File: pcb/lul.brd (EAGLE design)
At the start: 90 x 96 mm, 86 parts, among them IC1 STM32F072C8T6, IC2 REG1117, IC3 74AHCT1G08DBV, U1 UG-2864HSWEG01

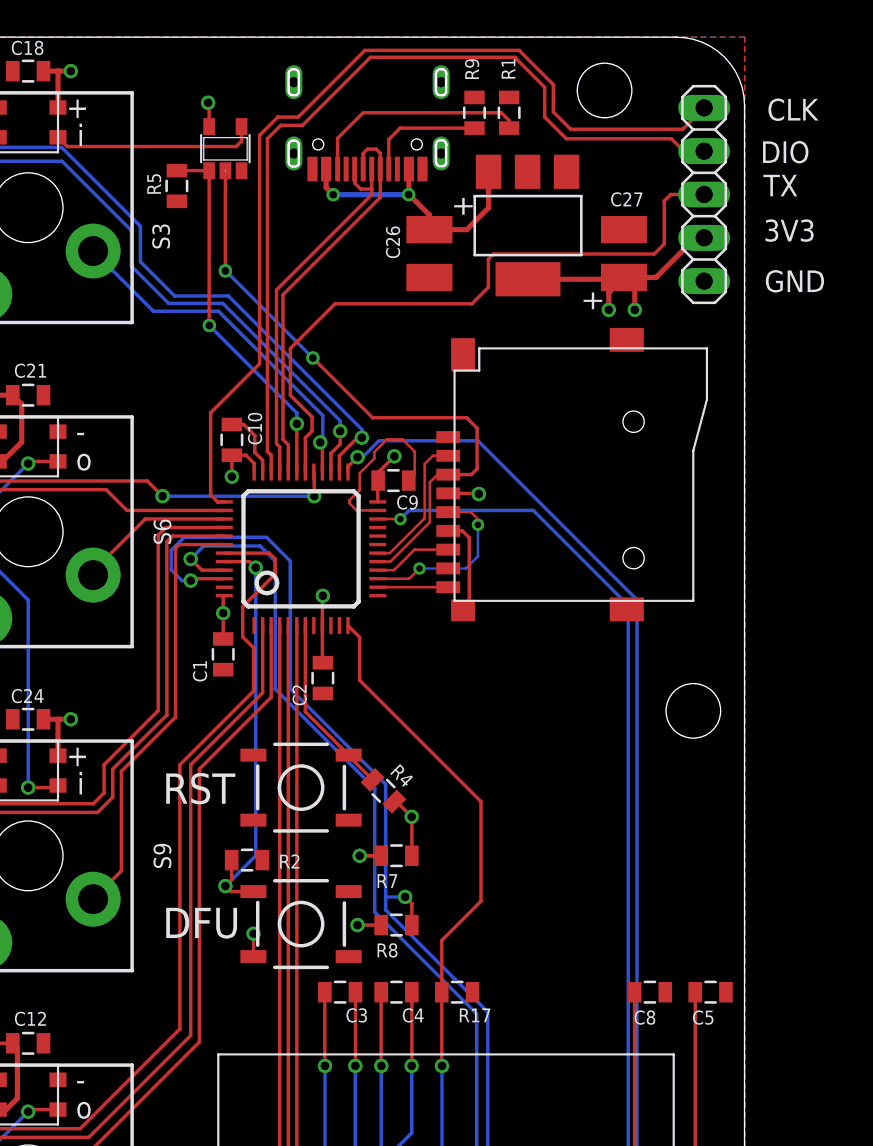
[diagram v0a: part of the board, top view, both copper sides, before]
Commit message: replaced DFU and RST button
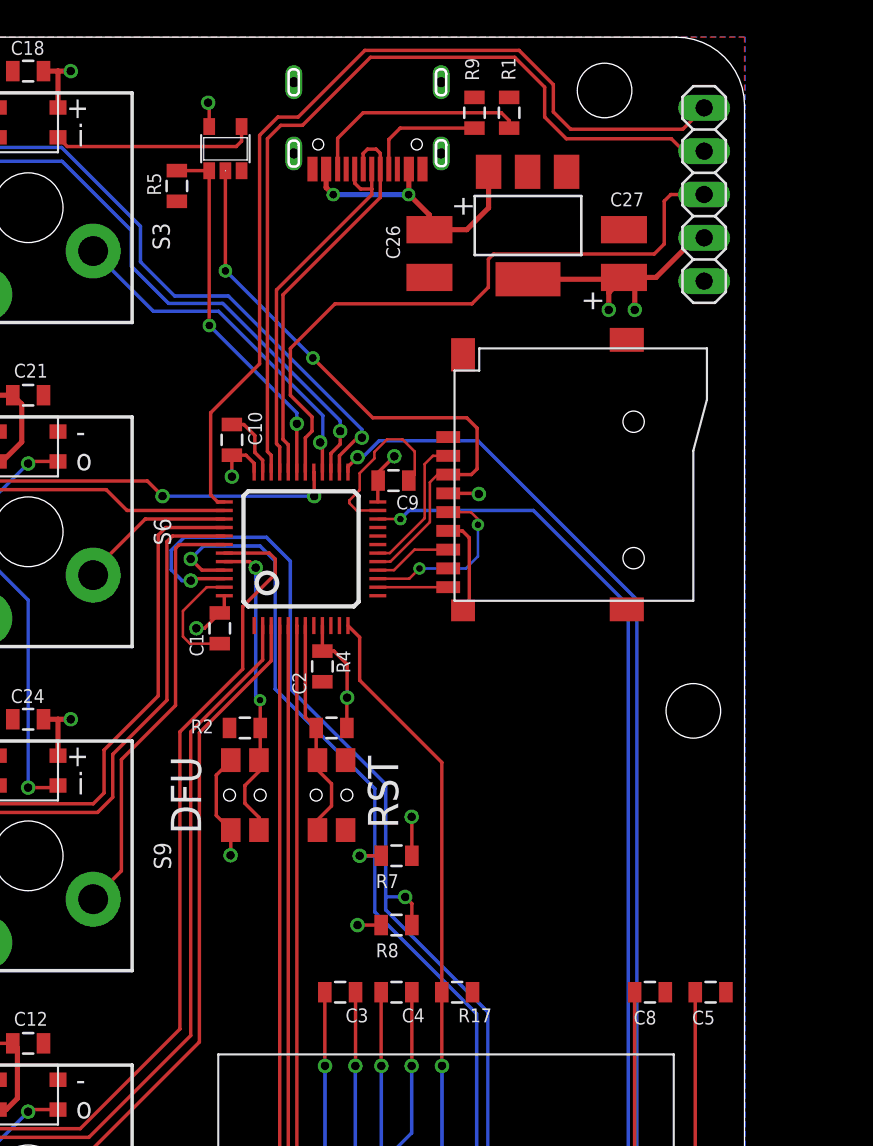
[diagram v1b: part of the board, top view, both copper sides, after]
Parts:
- removed S21, S22: TAC_SWITCHSMD, clock:TACTILE-SWITCH-SMD
- added SW1, SW2: 324_SW324_SWITCH_FOOT_HOLE, 3pos_slide_switch:342_SWICH_FOOT_HOLE
- moved R2 7.75 mm to (60.7, 55.5), turned to 0 degrees
- moved R4 4.78 mm to (65.8, 55.5), turned to 0 degrees
- moved C1 1.54 mm to (59.2, 61.3)
- moved C2 0.69 mm to (65.3, 59.1)
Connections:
- net +3V3: now also SW1.P$1, SW1.P$4; no longer S22.3
- net GND: now also SW2.P$2, SW2.P$3; no longer S21.4
- net N$2: now also SW1.P$2, SW1.P$3; no longer S22.1
- net RST: now also SW2.P$1, SW2.P$4; no longer S21.2
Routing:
- net +3V3: track 117.8 -> 124.7 mm
- net GND: track 48.6 -> 55.4 mm
- net N$2: track 24.8 -> 18.1 mm
- net RST: track 10.7 -> 13.0 mm
- net OLED_RESET: track 45.2 -> 43.3 mm
- net SW10: track 81.3 -> 80.8 mm
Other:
- board text added: "dekuNukem PT2 JUN19"
- board text removed: "dekuNukem 2017"

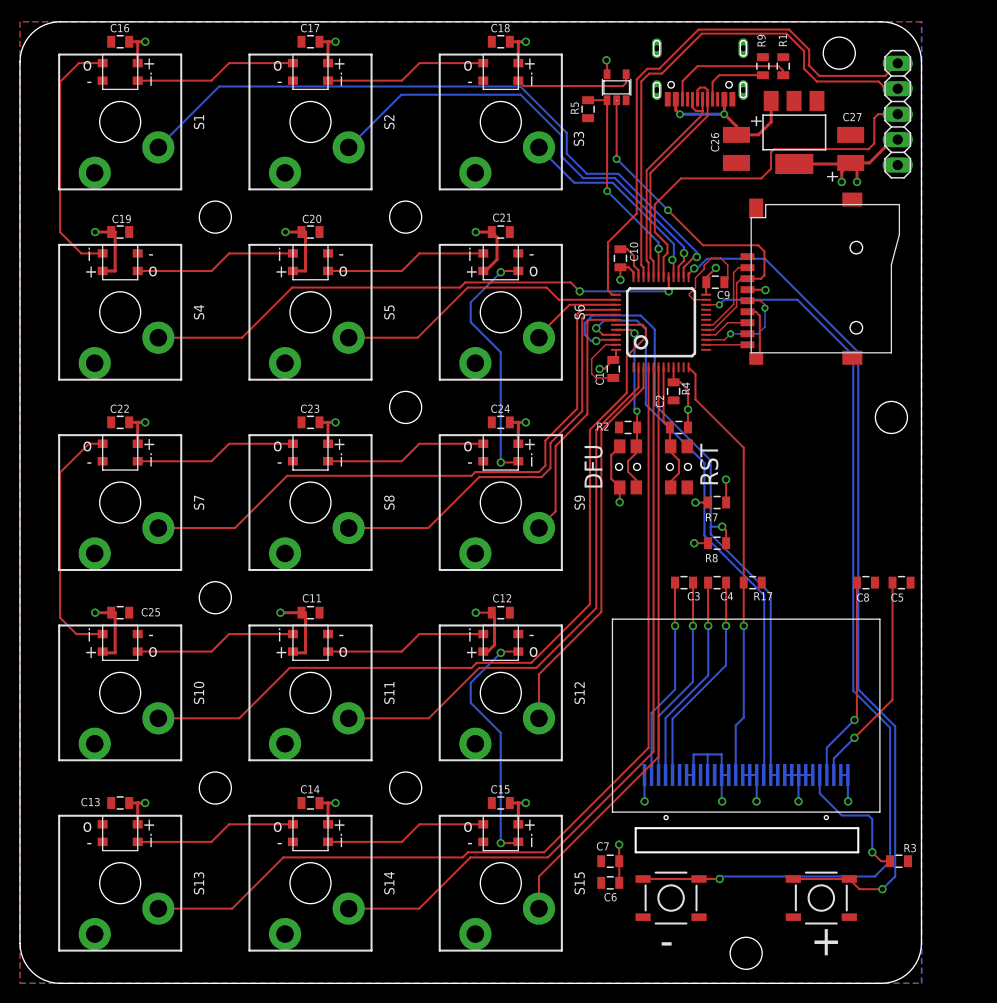
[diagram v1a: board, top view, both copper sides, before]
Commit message: new oled socket
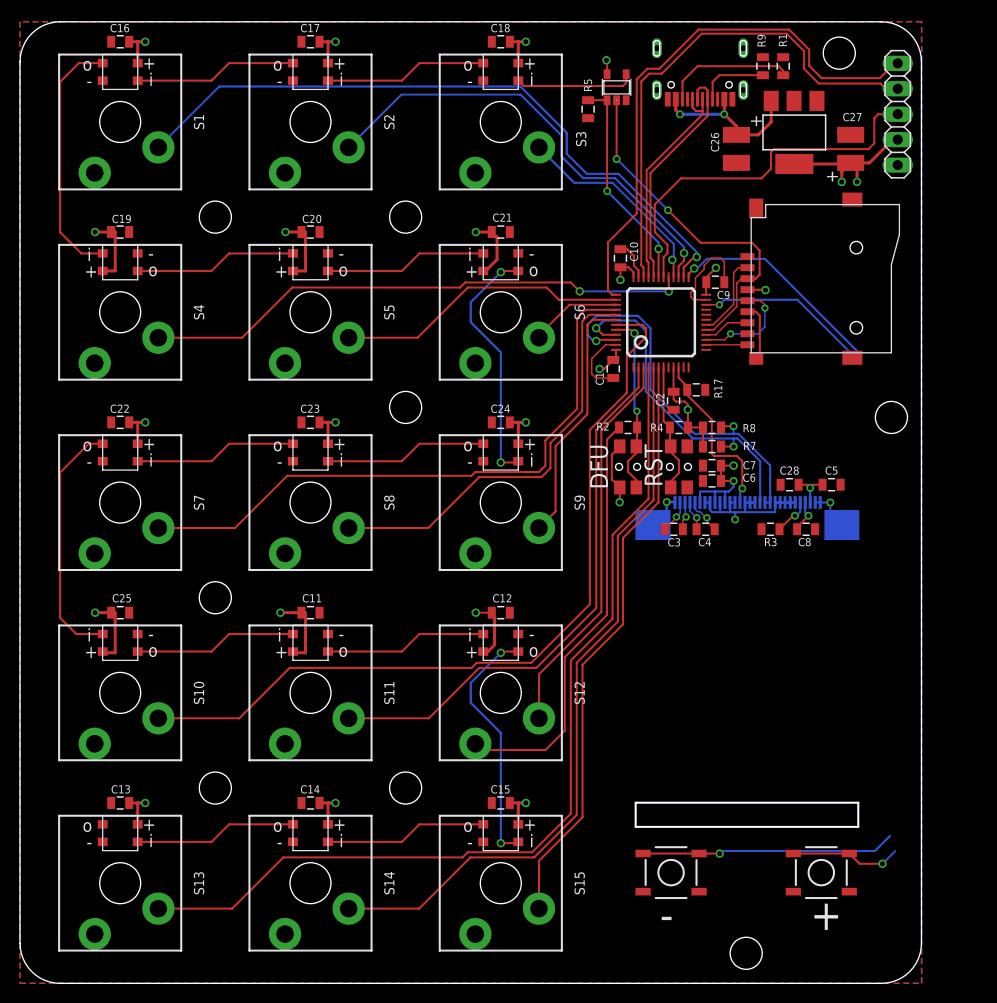
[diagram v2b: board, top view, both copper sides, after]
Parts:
- added C28: 1uF, clock:0805@1
- C7: value 1uF -> 2.2uF
- U1: device lul:UG-2864HSWEG01_0.96IN_WRAPAROUND -> lul:LUL_UG-2864HSWEG01_1.3_WRAPAROUND
- moved C6 41.4 mm to (69.1, 50.2)
- moved C7 40.8 mm to (69.1, 51.7)
- moved R3 35.5 mm to (74.9, 45.3), turned to 0 degrees
- moved U1 26.0 mm to (72.6, 48.0)
- moved R17 20.1 mm to (67.5, 59.3)
- moved C5 12.0 mm to (81.0, 49.8)
- moved R8 11.6 mm to (69.1, 55.5)
- moved C8 8.01 mm to (78.5, 45.3)
- moved R7 5.61 mm to (69.1, 53.6), turned to 180 degrees
- moved C4 5.46 mm to (68.5, 45.3)
- moved C3 5.43 mm to (65.3, 45.3)
- moved S19 2.54 mm to (80.0, 11.1)
- moved S20 2.54 mm to (65.0, 11.1)
- moved C2 0.94 mm to (65.3, 58.2)
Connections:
- net GND: now also C28.1, U1.31, U1.32
- net N$11: now also C28.2
- net OLED_RESET: now also IC1.10; no longer IC1.12
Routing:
- net BUTTON1: track 86.7 -> 32.9 mm
- net BUTTON2: track 94.6 -> 42.6 mm
- net GND: track 55.4 -> 92.8 mm, vias 5 -> 3
- net SDA: track 65.4 -> 38.8 mm
- net OLED_RESET: track 43.3 -> 17.6 mm
- net SCL: track 59.4 -> 34.5 mm
- net N$6: track 21.0 -> 2.95 mm
- net N$5: track 20.6 -> 2.84 mm
- net N$7: track 21.4 -> 3.66 mm
- net N$11: track 21.6 -> 4.12 mm
- net N$12: track 20.4 -> 3.27 mm
- net N$4: track 20.2 -> 3.29 mm
- net N$3: track 13.6 -> 3.72 mm
- net +3V3: track 124.7 -> 132.2 mm, vias 27 -> 26
- net SPI_MOSI: track 36.3 -> 35.3 mm
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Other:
- outline, holes or cut-outs redrawn

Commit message: new buttons
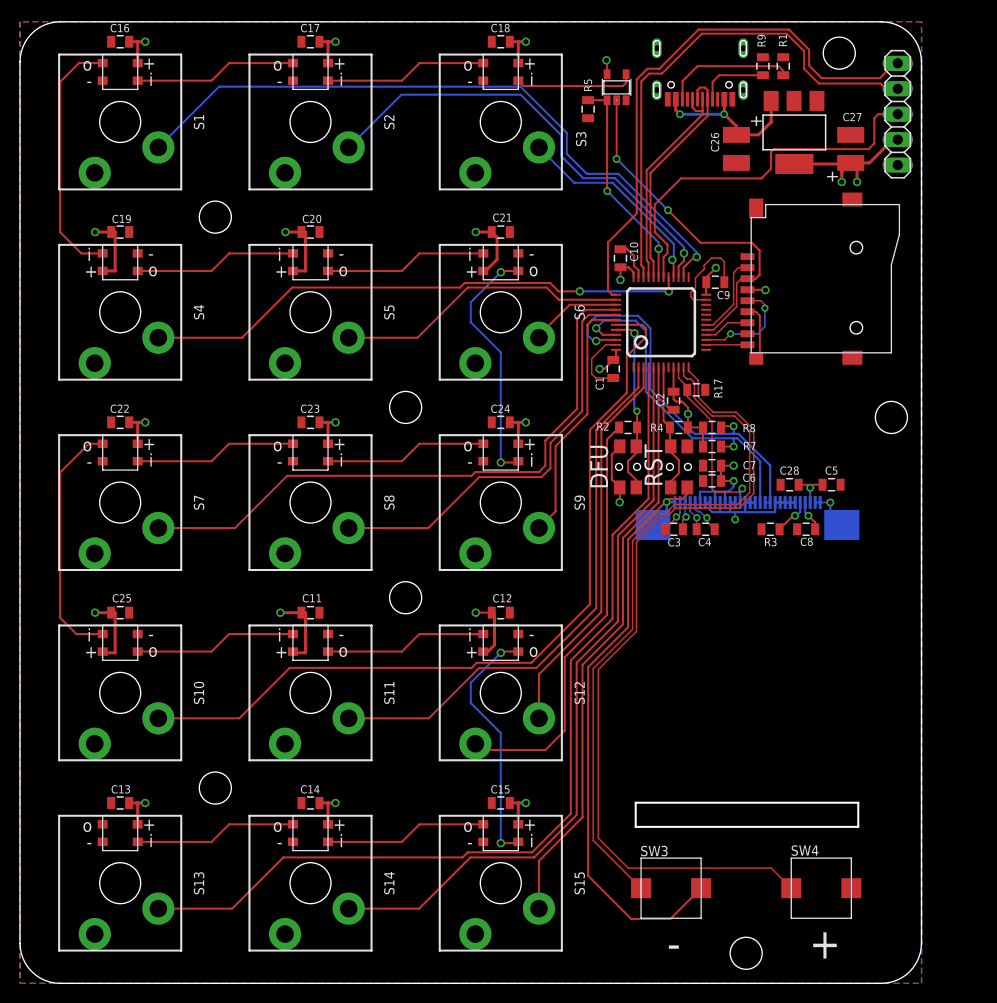
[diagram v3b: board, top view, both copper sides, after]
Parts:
- removed S19, S20: TAC_SWITCHSMD, clock:TACTILE-SWITCH-SMD
- removed U$12, U$13: M3_MOUNTING_HOLE, clock:M3_MOUNTING_HOLE_PACK
- added SW3, SW4: 6X6_SW, lul:6X6_SW_FOOT
- moved U$16 19.0 mm to (38.5, 38.5)
- turned C8 to 0 degrees
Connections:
- net BUTTON1: now also IC1.11, SW3.P$1; no longer IC1.25, S19.1, S19.2
- net BUTTON2: now also IC1.12, SW4.P$1; no longer IC1.22, S20.1, S20.2
- net GND: now also SW3.P$2, SW4.P$2; no longer S19.3, S19.4, S20.3, S20.4
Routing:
- net GND: track 92.8 -> 150.8 mm
- net BUTTON2: track 42.6 -> 82.8 mm, vias 2 -> 0
- net BUTTON1: track 32.9 -> 68.7 mm, vias 2 -> 0
- net OLED_RESET: track 17.6 -> 18.3 mm

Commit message: clean up main folder
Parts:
- C1, C10, C11, C12, C13, C14, C15, C16, C17, C18, C19, C2, C20, C21, C22, C23, C24, C25, C9: value 0.1uF -> 100nF
- C8: value 2.2uF/16V -> 2.2uF
- R2, R4, R5: value 10k -> 10K
- R7, R8: value 4K7 -> 5.1K
- S1, S10, S11, S12, S13, S14, S15, S2, S3, S4, S5, S6, S7, S8, S9: value MOMENTARY-SWITCH-SPST-LED-PTH-CHERRY -> CHERRY-MX-LED; device lul:CHERRY-MX-LED -> SparkFun-Cherry-MX-Switch-Breakout:CHERRY-MX-LED
- moved U$8 5.07 mm to (67.9, 92.2)
- moved U$9 1.41 mm to (86.0, 57.5)
- moved U$14 1.00 mm to (72.5, 4.00)
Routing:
- net SW1: track 67.5 -> 69.4 mm
- net SW2: track 46.4 -> 48.2 mm
- net GND: track 150.8 -> 149.1 mm
- net SW9: track 25.3 -> 26.2 mm
- net N$17: track 25.2 -> 26.0 mm
- net N$23: track 24.9 -> 25.7 mm
- net SW6: track 9.19 -> 9.83 mm
- net SW15: track 59.0 -> 59.5 mm
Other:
- board text added: "git.io/kbord"

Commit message: adjust components
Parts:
- moved C3 4.72 mm to (69.1, 48.1)
- moved C4 4.64 mm to (72.2, 48.1), turned to 0 degrees
- moved R3 2.90 mm to (75.7, 48.1)
- moved C8 2.81 mm to (78.7, 48.1)
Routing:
- net N$6: track 2.95 -> 8.59 mm
- net N$5: track 2.84 -> 5.84 mm
- net BUTTON1: track 68.7 -> 71.0 mm
- net BUTTON2: track 82.8 -> 85.1 mm
- net N$7: track 3.66 -> 5.70 mm
- net N$4: track 3.29 -> 5.19 mm

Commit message: new pcb ready for fab
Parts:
- removed C26: 47uF, clock:C1210
- added C29: 100nF, clock:0805@1
- moved U$10 0.72 mm to (82.5, 93.0)
- moved U$9 0.50 mm to (86.5, 57.5)
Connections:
- net GND: now also C29.1; no longer C26.2
- net N$1: now also C29.2; no longer C26.1
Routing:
- net N$1: track 16.4 -> 13.6 mm
- net UART1_TX: track 38.3 -> 39.1 mm
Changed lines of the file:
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@@
 <setting verticaltext="up"/>
 </settings>
-<grid distance="1" unitdist="mil" unit="mil" style="lines" multiple="1" display="yes" altdistance="5" altunitdist="mil" altunit="mil"/>
+<grid distance="1" unitdist="mil" unit="mm" style="lines" multiple="1" display="yes" altdistance="5" altunitdist="mil" altunit="mil"/>
 <layers>
 <layer number="1" name="Top" color="4" fill="1" visible="yes" active="yes"/>
@@
 <text x="57.8104" y="51.5874" size="1.778" layer="25" rot="R90" align="center">DFU</text>
 <text x="63.246" y="51.689" size="1.778" layer="25" rot="R270" align="center">RST</text>
-<text x="80.3656" y="4" size="3.048" layer="25" align="center">+</text>
-<text x="65.278" y="4" size="3.048" layer="25" align="center">-</text>
+<text x="80.3656" y="4.508" size="3.048" layer="25" align="center">+</text>
+<text x="65.278" y="4.508" size="3.048" layer="25" align="center">-</text>
 <text x="88.646" y="66.7766" size="2.1844" layer="26" rot="MR0">dekuNukem
 PT2 JUN19</text>
@@
 </element>
 <element name="C8" library="clock" package="0805@1" value="2.2uF" x="78.74" y="48.133" smashed="yes">
-<attribute name="NAME" x="79.4258" y="46.1391" size="0.8128" layer="25" rot="R180"/>
+<attribute name="NAME" x="82.9056" y="48.4251" size="0.8128" layer="25" rot="R180"/>
 </element>
 <element name="C6" library="clock" package="0805@1" value="1uF" x="69.088" y="50.165" smashed="yes">
@@
 </element>
 <element name="U$7" library="clock" package="M3_MOUNTING_HOLE_PACK" value="M3_MOUNTING_HOLE" x="19.5" y="19.5"/>
-<element name="U$9" library="clock" package="M3_MOUNTING_HOLE_PACK" value="M3_MOUNTING_HOLE" x="86" y="57.5"/>
-<element name="U$10" library="clock" package="M3_MOUNTING_HOLE_PACK" value="M3_MOUNTING_HOLE" x="81.795" y="92.873"/>
+<element name="U$9" library="clock" package="M3_MOUNTING_HOLE_PACK" value="M3_MOUNTING_HOLE" x="86.5" y="57.5"/>
+<element name="U$10" library="clock" package="M3_MOUNTING_HOLE_PACK" value="M3_MOUNTING_HOLE" x="82.5" y="93"/>
 <element name="U$11" library="clock" package="M3_MOUNTING_HOLE_PACK" value="M3_MOUNTING_HOLE" x="19.5" y="76.5"/>
 <element name="U$14" library="clock" package="M3_MOUNTING_HOLE_PACK" value="M3_MOUNTING_HOLE" x="72.5" y="4"/>
@@
 <attribute name="VALUE" x="75.565" y="90.551" size="0.4064" layer="27" rot="R90"/>
 </element>
-<element name="C26" library="clock" package="C1210" value="47uF" x="71.5264" y="83.312" rot="R270"/>
 <element name="SW2" library="3pos_slide_switch" package="342_SWICH_FOOT_HOLE" value="324_SW324_SWITCH_FOOT_HOLE" x="65.786" y="51.562" smashed="yes" rot="R270"/>
 <element name="SW1" library="3pos_slide_switch" package="342_SWICH_FOOT_HOLE" value="324_SW324_SWITCH_FOOT_HOLE" x="60.706" y="51.562" smashed="yes" rot="R270"/>
@@
 <attribute name="NAME" x="76.952" y="12.7512" size="1.016" layer="25"/>
 </element>
+<element name="C29" library="clock" package="0805@1" value="100nF" x="72.517" y="85.0138" rot="R90"/>
 </elements>
 <signals>
@@
 <contactref element="U$8" pad="P$13"/>
 <contactref element="U$8" pad="B11A12"/>
-<contactref element="C26" pad="2"/>
 <wire x1="61.75" y1="70.5" x2="61.75" y2="71.1936" width="0.2032" layer="1"/>
 <wire x1="61.75" y1="71.1936" x2="61.2902" y2="71.6534" width="0.2032" layer="1"/>
@@
 <wire x1="72.8726" y1="47.0408" x2="72.8726" y2="45.8216" width="0.2032" layer="16"/>
 <wire x1="72.8726" y1="47.0408" x2="72.7456" y2="47.0408" width="0.2032" layer="16"/>
+<contactref element="C29" pad="1"/>
 </signal>
 <signal name="SCL">
@@
 <wire x1="64.643" y1="72.898" x2="64.643" y2="73.7362" width="0.2032" layer="1"/>
 <wire x1="64.643" y1="73.7362" x2="63.373" y2="75.0062" width="0.2032" layer="1"/>
-<wire x1="63.373" y1="75.0062" x2="63.373" y2="77.7494" width="0.2032" layer="1"/>
-<wire x1="63.373" y1="77.7494" x2="65.9892" y2="80.3656" width="0.2032" layer="1"/>
-<wire x1="65.9892" y1="80.3656" x2="73.787" y2="80.3656" width="0.2032" layer="1"/>
-<wire x1="73.787" y1="80.3656" x2="74.7268" y2="81.3054" width="0.2032" layer="1"/>
-<wire x1="74.7268" y1="81.3054" x2="74.7268" y2="82.804" width="0.2032" layer="1"/>
-<wire x1="74.7268" y1="82.804" x2="75.1078" y2="83.185" width="0.2032" layer="1"/>
-<wire x1="75.1078" y1="83.185" x2="84.6074" y2="83.185" width="0.2032" layer="1"/>
+<wire x1="63.373" y1="75.0062" x2="63.373" y2="80.5688" width="0.2032" layer="1"/>
+<wire x1="63.373" y1="80.5688" x2="65.9892" y2="83.185" width="0.2032" layer="1"/>
+<wire x1="65.9892" y1="83.185" x2="84.6074" y2="83.185" width="0.2032" layer="1"/>
 <wire x1="84.6074" y1="83.185" x2="85.2932" y2="83.8708" width="0.2032" layer="1"/>
 <wire x1="85.2932" y1="83.8708" x2="85.2932" y2="86.3854" width="0.2032" layer="1"/>
@@
 <wire x1="71.5518" y1="69.9008" x2="72.0038" y2="70.3528" width="0.1524" layer="1"/>
 <wire x1="72.6274" y1="70.3528" x2="73.4516" y2="70.3528" width="0.2032" layer="1"/>
-<wire x1="73.4516" y1="70.3528" x2="73.8378" y2="70.739" width="0.2032" layer="1"/>
-<wire x1="73.8378" y1="70.739" x2="73.8378" y2="73.1774" width="0.2032" layer="1"/>
-<wire x1="73.8378" y1="73.1774" x2="73.0758" y2="73.9394" width="0.2032" layer="1"/>
-<wire x1="73.0758" y1="73.9394" x2="67.945" y2="73.9394" width="0.2032" layer="1"/>
+<wire x1="73.4516" y1="70.3528" x2="73.9648" y2="70.866" width="0.2032" layer="1"/>
+<wire x1="73.9648" y1="70.866" x2="73.9648" y2="73.3552" width="0.2032" layer="1"/>
+<wire x1="73.9648" y1="73.3552" x2="73.3806" y2="73.9394" width="0.2032" layer="1"/>
+<wire x1="73.3806" y1="73.9394" x2="67.945" y2="73.9394" width="0.2032" layer="1"/>
 <wire x1="67.945" y1="73.9394" x2="64.6938" y2="77.1906" width="0.2032" layer="1"/>
 <via x="64.6938" y="77.1906" extent="1-16" drill="0.45"/>
@@
 <contactref element="U$8" pad="A4B9"/>
 <contactref element="IC2" pad="3"/>
-<contactref element="C26" pad="1"/>
 <via x="65.8876" y="86.7664" extent="1-16" drill="0.45"/>
 <wire x1="65.8876" y1="86.7664" x2="70.3072" y2="86.7664" width="0.3048" layer="16"/>
 <via x="70.3072" y="86.7664" extent="1-16" drill="0.45"/>
-<wire x1="70.32" y1="86.7792" x2="71.5264" y2="85.5728" width="0.3048" layer="1"/>
-<wire x1="71.5264" y1="85.5728" x2="71.5264" y2="84.712" width="0.3048" layer="1"/>
-<wire x1="71.5264" y1="84.712" x2="73.7138" y2="84.712" width="0.3048" layer="1"/>
-<wire x1="74.9946" y1="85.9928" x2="74.9946" y2="88.1046" width="0.3048" layer="1"/>
-<wire x1="73.7138" y1="84.712" x2="74.9946" y2="85.9928" width="0.3048" layer="1"/>
 <wire x1="70.32" y1="86.7792" x2="70.3072" y2="86.7664" width="0.3048" layer="1"/>
 <wire x1="65.4438" y1="88.3037" x2="65.4438" y2="87.2102" width="0.254" layer="1"/>
@@
 <wire x1="70.2938" y1="88.3037" x2="70.2938" y2="86.8054" width="0.254" layer="1"/>
 <wire x1="70.2938" y1="86.8054" x2="70.32" y2="86.7792" width="0.254" layer="1"/>
+<contactref element="C29" pad="2"/>
+<wire x1="70.3072" y1="86.7664" x2="71.1598" y2="85.9138" width="0.254" layer="1"/>
+<wire x1="71.1598" y1="85.9138" x2="72.517" y2="85.9138" width="0.254" layer="1"/>
+<wire x1="74.9946" y1="88.1046" x2="72.8038" y2="85.9138" width="0.254" layer="1"/>
+<wire x1="72.8038" y1="85.9138" x2="72.517" y2="85.9138" width="0.254" layer="1"/>
 </signal>
 <signal name="DNDNDN">
